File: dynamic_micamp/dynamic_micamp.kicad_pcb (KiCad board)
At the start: 2 copper layers, 72 x 47 mm, 20 parts, among them J1 AudioJack3_123, J2 USB_B_Micro, J3 AudioJack3_123, U1 NJM4580

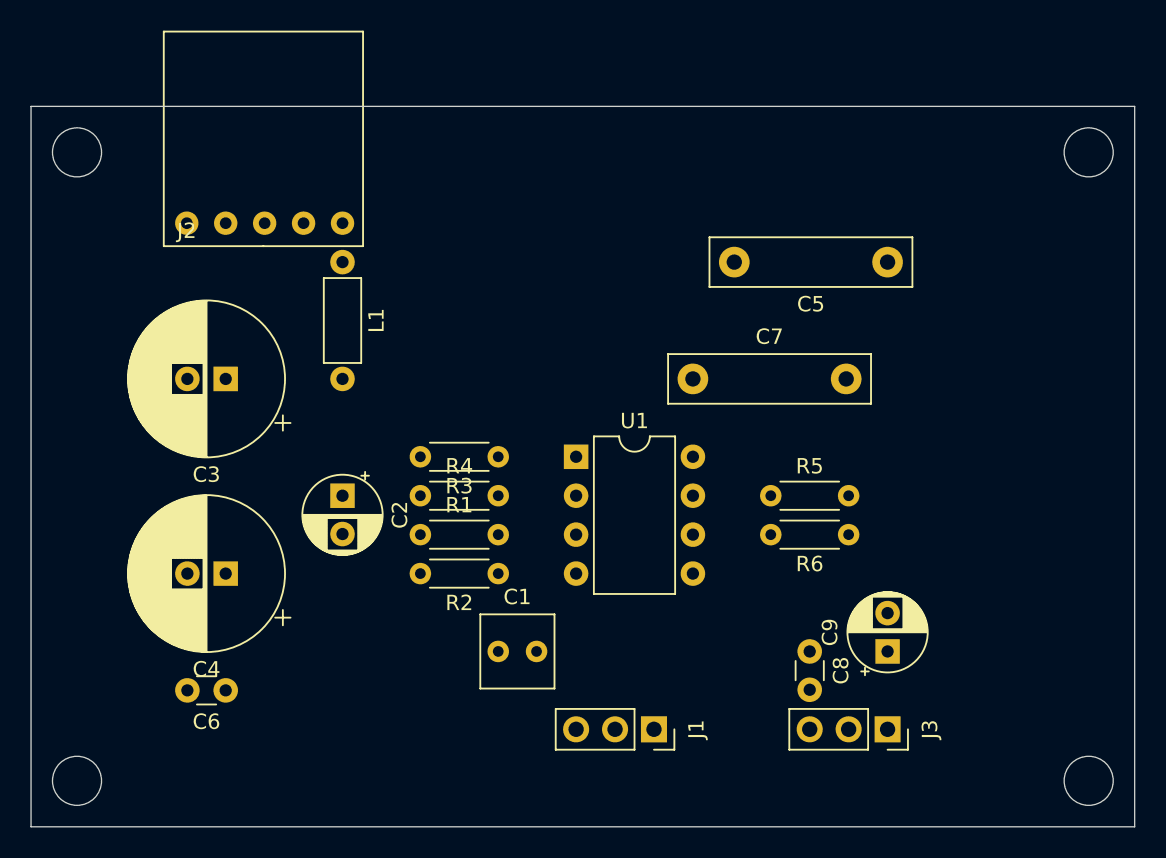
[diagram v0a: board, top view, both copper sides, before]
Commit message: resize C3 to learger one
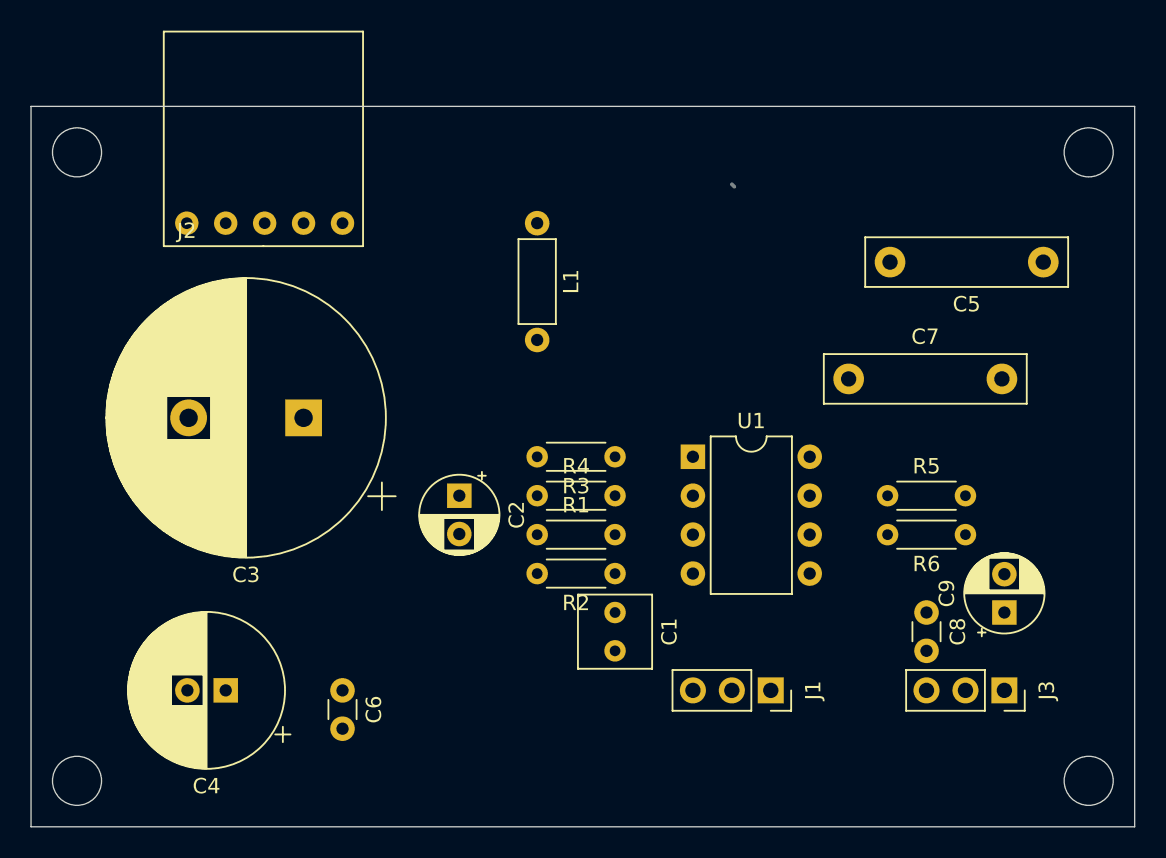
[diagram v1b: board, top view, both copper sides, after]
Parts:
- C3: footprint Capacitor_THT:CP_Radial_D10.0mm_P2.50mm -> Capacitor_THT:CP_Radial_D18.0mm_P7.50mm
- moved L1 13.0 mm to (63.0, 37.6)
- moved C5 10.2 mm to (96.0, 40.2)
- moved C7 10.2 mm to (83.3, 47.8)
- moved J1 8.03 mm to (78.3, 68.1)
- moved J3 8.03 mm to (93.5, 68.1)
- moved C8 8.03 mm to (88.4, 63.0)
- moved C9 8.03 mm to (93.5, 63.0)
- moved C1 8.03 mm to (68.1, 63.0), turned to 270 degrees
- moved R1 7.62 mm to (63.0, 57.9)
- moved R4 7.62 mm to (63.0, 55.4)
- moved U1 7.62 mm to (73.2, 52.9)
- moved C2 7.62 mm to (57.9, 55.4)
- moved C4 7.62 mm to (42.7, 68.1)
- moved C6 7.62 mm to (50.3, 68.1), turned to 270 degrees
- moved R2 7.62 mm to (68.1, 60.5)
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
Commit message: done
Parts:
- moved J1 10.2 mm to (68.1, 68.1), turned to 90 degrees
- moved R6 5.08 mm to (85.9, 57.9), turned to 0 degrees
- moved C9 2.54 mm to (91.0, 63.0), turned to 0 degrees
- moved L1 2.54 mm to (60.5, 37.6)
- moved R3 2.54 mm to (70.6, 52.9)
- moved C2 2.54 mm to (55.4, 55.4)
- moved R4 2.54 mm to (65.6, 55.4)
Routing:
- net GND: track 0.34 -> 175.6 mm
- net VCC: track 0.00 -> 96.5 mm, vias 0 -> 2
- net Net-(R4-Pad1): track 0.00 -> 31.1 mm, vias 0 -> 2
- net Net-(C7-Pad1): track 0.00 -> 30.5 mm, vias 0 -> 2
- net Net-(C7-Pad2): track 0.00 -> 24.7 mm
- net Net-(C5-Pad1): track 0.00 -> 20.3 mm
- net Net-(C2-Pad1): track 0.00 -> 15.2 mm
- net Net-(C1-Pad1): track 0.00 -> 10.2 mm
- net Net-(J2-Pad1): track 0.00 -> 10.2 mm
- net Net-(C9-Pad2): track 0.00 -> 7.64 mm
- net Net-(C1-Pad2): track 0.00 -> 5.12 mm
- net Net-(R3-Pad1): track 0.00 -> 5.08 mm
